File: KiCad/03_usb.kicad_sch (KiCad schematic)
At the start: 18 parts, among them IC301 CP2102N-A02-GQFN28R, J301 USB_C_Receptacle_USB2.0, J302 USB_C_Receptacle_USB2.0, U301 USBLC6-2SC6, U302 USBLC6-2SC6

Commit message: BOM updates
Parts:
- C303, C304: footprint Capacitor_SMD:C_0402_1005Metric -> Capacitor_SMD:C_0603_1608Metric; Manufacturer Part Number CL05B104KO5NNNC -> CL10B104KB8NNNC
- IC301: Manufacturer (none) -> SILICON LABS; Manufacturer Part Number (none) -> CP2102N-A02-GQFN28R
- R303, R304, R305, R306: footprint Resistor_SMD:R_0402_1005Metric -> Resistor_SMD:R_0805_2012Metric; Manufacturer Part Number 0402WGF5101TCE -> 0805W8F5101T5E
- R307: Manufacturer Part Number 0805W8D4752T5E -> TC0525B4752T5G
- R308: footprint Resistor_SMD:R_0603_1608Metric -> Resistor_SMD:R_0805_2012Metric; Manufacturer Part Number 0603WAF1004T5E -> 0805W8F1004T5E
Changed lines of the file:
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@@
 			)
 		)
-		(property "Footprint" "Resistor_SMD:R_0402_1005Metric"
+		(property "Footprint" "Resistor_SMD:R_0805_2012Metric"
 			(at 127.762 54.61 90)
 			(effects
@@
 			)
 		)
-		(property "Manufacturer Part Number" "0402WGF5101TCE"
+		(property "Manufacturer Part Number" "0805W8F5101T5E"
 			(at 129.54 54.61 0)
 			(effects
@@
 			)
 		)
-		(property "Footprint" "Resistor_SMD:R_0402_1005Metric"
+		(property "Footprint" "Resistor_SMD:R_0805_2012Metric"
 			(at 118.872 54.61 90)
 			(effects
@@
 			)
 		)
-		(property "Manufacturer Part Number" "0402WGF5101TCE"
+		(property "Manufacturer Part Number" "0805W8F5101T5E"
 			(at 120.65 54.61 0)
 			(effects
@@
 			)
 		)
-		(property "Footprint" "Resistor_SMD:R_0402_1005Metric"
+		(property "Footprint" "Resistor_SMD:R_0805_2012Metric"
 			(at 212.852 54.61 90)
 			(effects
@@
 			)
 		)
-		(property "Manufacturer Part Number" "0402WGF5101TCE"
+		(property "Manufacturer Part Number" "0805W8F5101T5E"
 			(at 214.63 54.61 0)
 			(effects
@@
 			)
 		)
-		(property "Footprint" "Resistor_SMD:R_0402_1005Metric"
+		(property "Footprint" "Resistor_SMD:R_0805_2012Metric"
 			(at 221.742 54.61 90)
 			(effects
@@
 			)
 		)
-		(property "Manufacturer Part Number" "0402WGF5101TCE"
+		(property "Manufacturer Part Number" "0805W8F5101T5E"
 			(at 223.52 54.61 0)
 			(effects
@@
 			)
 		)
-		(property "Footprint" "Resistor_SMD:R_0603_1608Metric"
+		(property "Footprint" "Resistor_SMD:R_0805_2012Metric"
 			(at 35.56 173.228 90)
 			(effects
@@
 			)
 		)
-		(property "Manufacturer Part Number" "0603WAF1004T5E"
+		(property "Manufacturer Part Number" "0805W8F1004T5E"
 			(at 35.56 171.45 90)
 			(effects
@@
 			)
 		)
-		(property "Manufacturer Part Number" "0805W8D4752T5E"
+		(property "Manufacturer Part Number" "TC0525B4752T5G"
 			(at 82.55 62.23 0)
 			(effects
@@
 			)
 		)
-		(property "Footprint" "Capacitor_SMD:C_0402_1005Metric"
+		(property "Footprint" "Capacitor_SMD:C_0603_1608Metric"
 			(at 102.5652 59.69 0)
 			(effects
@@
 			)
 		)
-		(property "Manufacturer Part Number" "CL05B104KO5NNNC"
+		(property "Manufacturer Part Number" "CL10B104KB8NNNC"
 			(at 101.6 55.88 90)
 			(effects
@@
 			)
 		)
+		(property "Manufacturer" "SILICON LABS"
+			(at 54.61 60.96 0)
+			(effects
+				(font
+					(size 1.27 1.27)
+				)
+				(hide yes)
+			)
+		)
+		(property "Manufacturer Part Number" "CP2102N-A02-GQFN28R"
+			(at 54.61 60.96 0)
+			(effects
+				(font
+					(size 1.27 1.27)
+				)
+				(hide yes)
+			)
+		)
 		(pin "5"
 		)
@@
 			)
 		)
-		(property "Footprint" "Capacitor_SMD:C_0402_1005Metric"
+		(property "Footprint" "Capacitor_SMD:C_0603_1608Metric"
 			(at 201.6252 59.69 0)
 			(effects
@@
 			)
 		)
-		(property "Manufacturer Part Number" "CL05B104KO5NNNC"
+		(property "Manufacturer Part Number" "CL10B104KB8NNNC"
 			(at 200.66 55.88 90)
 			(effects

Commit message: BOM updates. First layout
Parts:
- C302, C303, C304: footprint Capacitor_SMD:C_0603_1608Metric -> Capacitor_SMD:C_0402_1005Metric; Manufacturer Part Number CL10B104KB8NNNC -> CL05B104KO5NNNC
- R301: footprint Resistor_SMD:R_0805_2012Metric -> Resistor_SMD:R_0402_1005Metric; Manufacturer Part Number 0805W8F1001T5E -> 0402WGF1001TCE
- R302: footprint Resistor_SMD:R_0805_2012Metric -> Resistor_SMD:R_0402_1005Metric; Manufacturer Part Number 0805W8D2212T5E -> 0402WGF2212TCE
- R303, R304, R305, R306: footprint Resistor_SMD:R_0805_2012Metric -> Resistor_SMD:R_0402_1005Metric; Manufacturer Part Number 0805W8F5101T5E -> 0402WGF5101TCE
- R307: footprint Resistor_SMD:R_0805_2012Metric -> Resistor_SMD:R_0402_1005Metric; Manufacturer Part Number TC0525B4752T5G -> 0402WGF4752TCE
- R308: footprint Resistor_SMD:R_0805_2012Metric -> Resistor_SMD:R_0603_1608Metric; Manufacturer Part Number 0805W8F1004T5E -> 0603WAF1004T5E
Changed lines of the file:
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@@
 		(on_board yes)
 		(dnp no)
-		(property "Reference" "#PWR0304"
+		(property "Reference" "#PWR0305"
 			(at 162.56 52.07 0)
 			(effects
@@
 			(project "esp32_s3_weather_webserver"
 				(path "/04e96486-ec4c-4881-a0bf-37cb6ce91c2d/03b8cdb9-87b3-40fb-b75a-b9ce0b7f30b6"
-					(reference "#PWR0304")
+					(reference "#PWR0305")
 					(unit 1)
 				)
@@
 			)
 		)
-		(property "Footprint" "Resistor_SMD:R_0805_2012Metric"
+		(property "Footprint" "Resistor_SMD:R_0402_1005Metric"
 			(at 127.762 54.61 90)
 			(effects
@@
 			)
 		)
-		(property "Manufacturer Part Number" "0805W8F5101T5E"
+		(property "Manufacturer Part Number" "0402WGF5101TCE"
 			(at 129.54 54.61 0)
 			(effects
@@
 			)
 		)
-		(property "Footprint" "Resistor_SMD:R_0805_2012Metric"
+		(property "Footprint" "Resistor_SMD:R_0402_1005Metric"
 			(at 118.872 54.61 90)
 			(effects
@@
 			)
 		)
-		(property "Manufacturer Part Number" "0805W8F5101T5E"
+		(property "Manufacturer Part Number" "0402WGF5101TCE"
 			(at 120.65 54.61 0)
 			(effects
@@
 			)
 		)
-		(property "Footprint" "Resistor_SMD:R_0805_2012Metric"
+		(property "Footprint" "Resistor_SMD:R_0402_1005Metric"
 			(at 212.852 54.61 90)
 			(effects
@@
 			)
 		)
-		(property "Manufacturer Part Number" "0805W8F5101T5E"
+		(property "Manufacturer Part Number" "0402WGF5101TCE"
 			(at 214.63 54.61 0)
 			(effects
@@
 			)
 		)
-		(property "Footprint" "Resistor_SMD:R_0805_2012Metric"
+		(property "Footprint" "Resistor_SMD:R_0402_1005Metric"
 			(at 221.742 54.61 90)
 			(effects
@@
 			)
 		)
-		(property "Manufacturer Part Number" "0805W8F5101T5E"
+		(property "Manufacturer Part Number" "0402WGF5101TCE"
 			(at 223.52 54.61 0)
 			(effects
@@
 		(on_board yes)
 		(dnp no)
-		(property "Reference" "#PWR0305"
+		(property "Reference" "#PWR0306"
 			(at 256.54 52.07 0)
 			(effects
@@
 			(project "esp32_s3_weather_webserver"
 				(path "/04e96486-ec4c-4881-a0bf-37cb6ce91c2d/03b8cdb9-87b3-40fb-b75a-b9ce0b7f30b6"
-					(reference "#PWR0305")
+					(reference "#PWR0306")
 					(unit 1)
 				)
@@
 			)
 		)
-		(property "Footprint" "Resistor_SMD:R_0805_2012Metric"
+		(property "Footprint" "Resistor_SMD:R_0402_1005Metric"
 			(at 69.088 52.07 90)
 			(effects
@@
 			)
 		)
-		(property "Manufacturer Part Number" "0805W8F1001T5E"
+		(property "Manufacturer Part Number" "0402WGF1001TCE"
 			(at 67.31 52.07 0)
 			(effects
@@
 			)
 		)
-		(property "Footprint" "Capacitor_SMD:C_0603_1608Metric"
+		(property "Footprint" "Capacitor_SMD:C_0402_1005Metric"
 			(at 35.2552 49.53 0)
 			(effects
@@
 			)
 		)
-		(property "Manufacturer Part Number" "CL10B104KB8NNNC"
+		(property "Manufacturer Part Number" "CL05B104KO5NNNC"
 			(at 34.29 45.72 0)
 			(effects
@@
 		(on_board yes)
 		(dnp no)
-		(property "Reference" "#PWR011"
+		(property "Reference" "#PWR0304"
 			(at 101.6 50.8 0)
 			(effects
@@
 			(project "esp32_s3_weather_webserver"
 				(path "/04e96486-ec4c-4881-a0bf-37cb6ce91c2d/03b8cdb9-87b3-40fb-b75a-b9ce0b7f30b6"
-					(reference "#PWR011")
+					(reference "#PWR0304")
 					(unit 1)
 				)
@@
 			)
 		)
-		(property "Footprint" "Resistor_SMD:R_0805_2012Metric"
+		(property "Footprint" "Resistor_SMD:R_0603_1608Metric"
 			(at 35.56 173.228 90)
 			(effects
@@
 			)
 		)
-		(property "Manufacturer Part Number" "0805W8F1004T5E"
+		(property "Manufacturer Part Number" "0603WAF1004T5E"
 			(at 35.56 171.45 90)
 			(effects
@@
 			)
 		)
-		(property "Footprint" "Resistor_SMD:R_0805_2012Metric"
+		(property "Footprint" "Resistor_SMD:R_0402_1005Metric"
 			(at 84.328 62.23 90)
 			(effects
@@
 			)
 		)
-		(property "Manufacturer Part Number" "TC0525B4752T5G"
+		(property "Manufacturer Part Number" "0402WGF4752TCE"
 			(at 82.55 62.23 0)
 			(effects
@@
 			)
 		)
-		(property "Footprint" "Capacitor_SMD:C_0603_1608Metric"
+		(property "Footprint" "Capacitor_SMD:C_0402_1005Metric"
 			(at 102.5652 59.69 0)
 			(effects
@@
 			)
 		)
-		(property "Manufacturer Part Number" "CL10B104KB8NNNC"
+		(property "Manufacturer Part Number" "CL05B104KO5NNNC"
 			(at 101.6 55.88 90)
 			(effects
@@
 			)
 		)
-		(property "Footprint" "Capacitor_SMD:C_0603_1608Metric"
+		(property "Footprint" "Capacitor_SMD:C_0402_1005Metric"
 			(at 201.6252 59.69 0)
 			(effects
@@
 			)
 		)
-		(property "Manufacturer Part Number" "CL10B104KB8NNNC"
+		(property "Manufacturer Part Number" "CL05B104KO5NNNC"
 			(at 200.66 55.88 90)
 			(effects
@@
 			)
 		)
-		(property "Footprint" "Resistor_SMD:R_0805_2012Metric"
+		(property "Footprint" "Resistor_SMD:R_0402_1005Metric"
 			(at 84.328 52.07 90)
 			(effects
@@
 			)
 		)
-		(property "Manufacturer Part Number" "0805W8D2212T5E"
+		(property "Manufacturer Part Number" "0402WGF2212TCE"
 			(at 82.55 52.07 0)
 			(effects

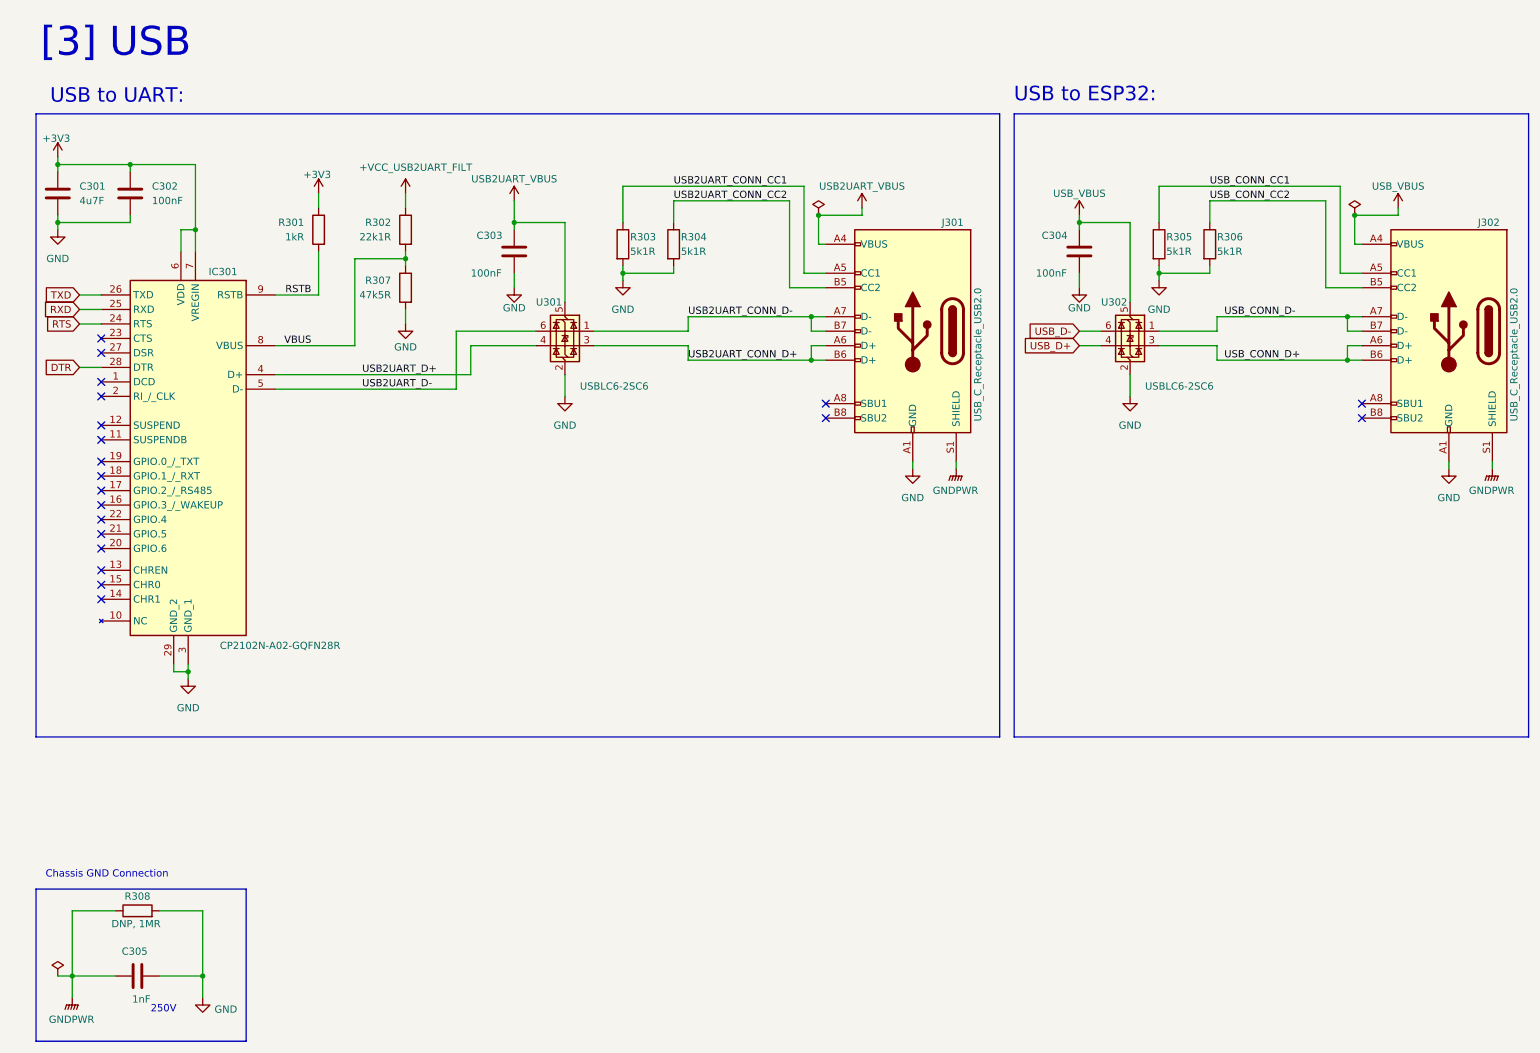
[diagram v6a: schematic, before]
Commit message: Remove broken scheme parts
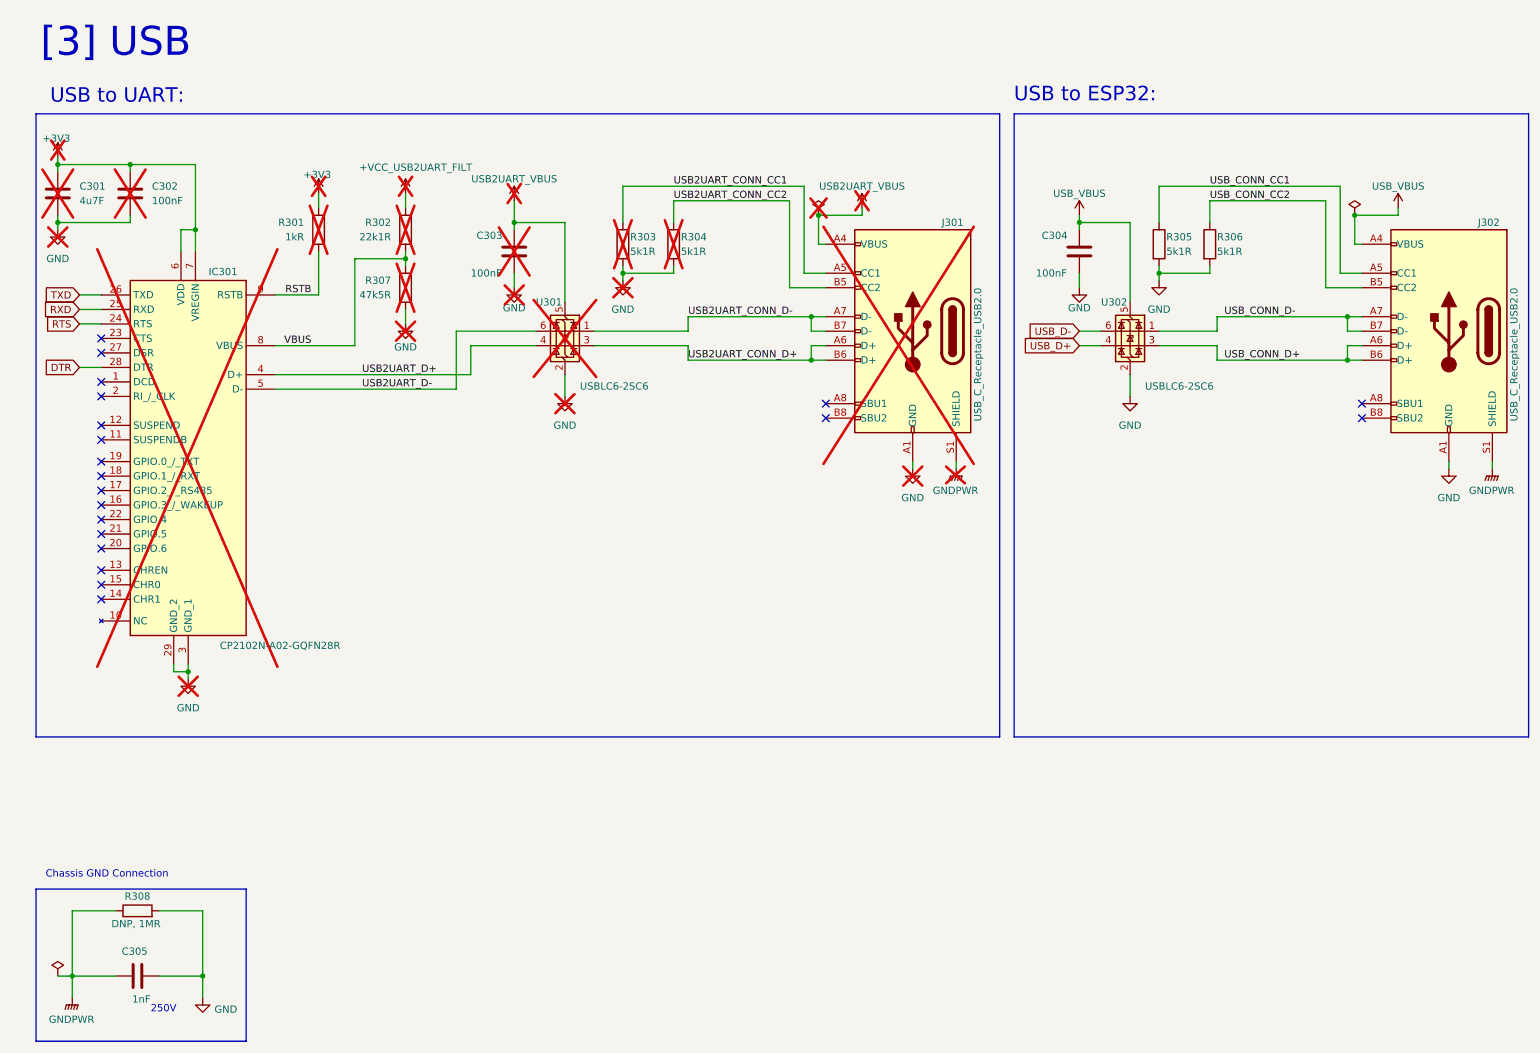
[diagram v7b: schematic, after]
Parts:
- C301, C302, C303, J301, R301, R302, R303, R304, R307, U301: now not fitted
- IC301: Manufacturer_Name Silicon Labs -> (none); Manufacturer_Part_Number CP2102N-A02-GQFN28R -> (none); Mouser Part Number 634-CP2102NA02QFN28R -> (none); Mouser Price/Stock https://www.mouser.co.uk/ProductDetail/Silicon-Labs/CP2102N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 -> (none); now not fitted
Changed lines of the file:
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@@
 		(exclude_from_sim no)
 		(in_bom yes)
-		(on_board yes)
-		(dnp no)
+		(on_board no)
+		(dnp yes)
 		(property "Reference" "J301"
 			(at 176.53 50.8 0)
@@
 		(in_bom yes)
 		(on_board yes)
-		(dnp no)
+		(dnp yes)
 		(property "Reference" "#PWR0305"
 			(at 162.56 52.07 0)
@@
 		(exclude_from_sim no)
 		(in_bom yes)
-		(on_board yes)
-		(dnp no)
+		(on_board no)
+		(dnp yes)
 		(property "Reference" "R304"
 			(at 130.81 53.34 0)
@@
 		(exclude_from_sim no)
 		(in_bom yes)
-		(on_board yes)
-		(dnp no)
+		(on_board no)
+		(dnp yes)
 		(property "Reference" "R303"
 			(at 121.92 53.34 0)
@@
 		(in_bom yes)
 		(on_board yes)
-		(dnp no)
+		(dnp yes)
 		(fields_autoplaced yes)
 		(property "Reference" "#PWR0316"
@@
 		(in_bom yes)
 		(on_board yes)
-		(dnp no)
+		(dnp yes)
 		(fields_autoplaced yes)
 		(property "Reference" "#PWR0309"
@@
 		(in_bom yes)
 		(on_board yes)
-		(dnp no)
+		(dnp yes)
 		(fields_autoplaced yes)
 		(property "Reference" "#PWR0308"
@@
 		(in_bom yes)
 		(on_board yes)
-		(dnp no)
+		(dnp yes)
 		(property "Reference" "#PWR0301"
 			(at 21.59 43.18 0)
@@
 		(in_bom yes)
 		(on_board yes)
-		(dnp no)
+		(dnp yes)
 		(property "Reference" "#PWR0303"
 			(at 82.55 49.53 0)
@@
 		(exclude_from_sim no)
 		(in_bom yes)
-		(on_board yes)
-		(dnp no)
+		(on_board no)
+		(dnp yes)
 		(fields_autoplaced yes)
 		(property "Reference" "R301"
@@
 			)
 		)
-		(property "MANUFACTURER" ""
-			(at 67.31 52.07 0)
-			(effects
-				(font
-					(size 1.27 1.27)
-				)
-				(hide yes)
-			)
-		)
 		(property "PARTREV" ""
 			(at 67.31 52.07 0)
@@
 		(in_bom yes)
 		(on_board yes)
-		(dnp no)
+		(dnp yes)
 		(property "Reference" "#PWR0302"
 			(at 67.31 49.53 0)
@@
 		(in_bom yes)
 		(on_board yes)
-		(dnp no)
+		(dnp yes)
 		(fields_autoplaced yes)
 		(property "Reference" "#PWR0317"
@@
 		(exclude_from_sim no)
 		(in_bom yes)
-		(on_board yes)
-		(dnp no)
+		(on_board no)
+		(dnp yes)
 		(fields_autoplaced yes)
 		(property "Reference" "C302"
@@
 			)
 		)
-		(property "MANUFACTURER" ""
-			(at 34.29 45.72 0)
-			(effects
-				(font
-					(size 1.27 1.27)
-				)
-				(hide yes)
-			)
-		)
 		(property "PARTREV" ""
 			(at 34.29 45.72 0)
@@
 		(in_bom yes)
 		(on_board yes)
-		(dnp no)
+		(dnp yes)
 		(property "Reference" "#PWR0311"
 			(at 101.6 68.58 0)
@@
 		(exclude_from_sim no)
 		(in_bom yes)
-		(on_board yes)
-		(dnp no)
+		(on_board no)
+		(dnp yes)
 		(property "Reference" "U301"
 			(at 107.696 64.77 0)
@@
 		(in_bom yes)
 		(on_board yes)
-		(dnp no)
+		(dnp yes)
 		(property "Reference" "#PWR0304"
 			(at 101.6 50.8 0)
@@
 		(in_bom yes)
 		(on_board yes)
-		(dnp no)
+		(dnp yes)
 		(fields_autoplaced yes)
 		(property "Reference" "#PWR0320"
@@
 		(in_bom yes)
 		(on_board yes)
-		(dnp no)
+		(dnp yes)
 		(fields_autoplaced yes)
 		(property "Reference" "#PWR0314"
@@
 		(in_bom yes)
 		(on_board yes)
-		(dnp no)
+		(dnp yes)
 		(property "Reference" "#PWR0313"
 			(at 82.55 74.93 0)
@@
 		(exclude_from_sim no)
 		(in_bom yes)
-		(on_board yes)
-		(dnp no)
+		(on_board no)
+		(dnp yes)
 		(fields_autoplaced yes)
 		(property "Reference" "C301"
@@
 			)
 		)
-		(property "MANUFACTURER" ""
-			(at 21.59 45.72 0)
-			(effects
-				(font
-					(size 1.27 1.27)
-				)
-				(hide yes)
-			)
-		)
 		(property "PARTREV" ""
 			(at 21.59 45.72 0)
@@
 		(exclude_from_sim no)
 		(in_bom yes)
-		(on_board yes)
-		(dnp no)
+		(on_board no)
+		(dnp yes)
 		(fields_autoplaced yes)
 		(property "Reference" "R307"
@@
 			)
 		)
-		(property "MANUFACTURER" ""
-			(at 82.55 62.23 0)
-			(effects
-				(font
-					(size 1.27 1.27)
-				)
-				(hide yes)
-			)
-		)
 		(property "PARTREV" ""
 			(at 82.55 62.23 0)
@@
 		(exclude_from_sim no)
 		(in_bom yes)
-		(on_board yes)
-		(dnp no)
+		(on_board no)
+		(dnp yes)
 		(property "Reference" "C303"
 			(at 94.996 53.086 0)
@@
 		(exclude_from_sim no)
 		(in_bom yes)
-		(on_board yes)
-		(dnp no)
+		(on_board no)
+		(dnp yes)
 		(property "Reference" "IC301"
 			(at 53.086 59.436 0)
@@
 			)
 		)
-		(property "Manufacturer_Name" "Silicon Labs"
-			(at 10.16 545.72 0)
-			(effects
-				(font
-					(size 1.27 1.27)
-				)
-				(justify left top)
-				(hide yes)
-			)
-		)
-		(property "Manufacturer_Part_Number" "CP2102N-A02-GQFN28R"
-			(at 10.16 645.72 0)
-			(effects
-				(font
-					(size 1.27 1.27)
-				)
-				(justify left top)
-				(hide yes)
-			)
-		)
-		(property "Mouser Part Number" "634-CP2102NA02QFN28R"
-			(at 10.16 745.72 0)
-			(effects
-				(font
-					(size 1.27 1.27)
-				)
-				(justify left top)
-				(hide yes)
-			)
-		)
-		(property "Mouser Price/Stock" "https://www.mouser.co.uk/ProductDetail/Silicon-Labs/CP2102N-A02-GQFN28R?qs=u16ybLDytRag4qKvSH3fTw%3D%3D"
-			(at 10.16 845.72 0)
-			(effects
-				(font
-					(size 1.27 1.27)
-				)
-				(justify left top)
-				(hide yes)
-			)
-		)
 		(property "Arrow Part Number" "CP2102N-A02-GQFN28R"
 			(at 10.16 945.72 0)
@@
 		(in_bom yes)
 		(on_board yes)
-		(dnp no)
+		(dnp yes)
 		(fields_autoplaced yes)
 		(property "Reference" "#FLG0301"
@@
 		(exclude_from_sim no)
 		(in_bom yes)
-		(on_board yes)
-		(dnp no)
+		(on_board no)
+		(dnp yes)
 		(fields_autoplaced yes)
 		(property "Reference" "R302"
@@
 			(at 82.55 52.07 0)
 			(effects
-				(font
-					(size 1.27 1.27)
-				)
-				(hide yes)
-			)
-		)
-		(property "MANUFACTURER" ""
-			(at 82.55 52.07 0)
-			(effects
